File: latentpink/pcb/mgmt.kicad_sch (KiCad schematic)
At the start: 82 parts, among them J10 XILINX_JTAG, J11 FAN_01, J12 FAN_01, J15 CONN_01X03, J16 JUMPER_0402_SPDT, J17 JUMPER_0402_SPDT, J23 PMOD_HOST, J7 RJ45, U2 XC7K160T-2FBG484C, U20 AT24MAC402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

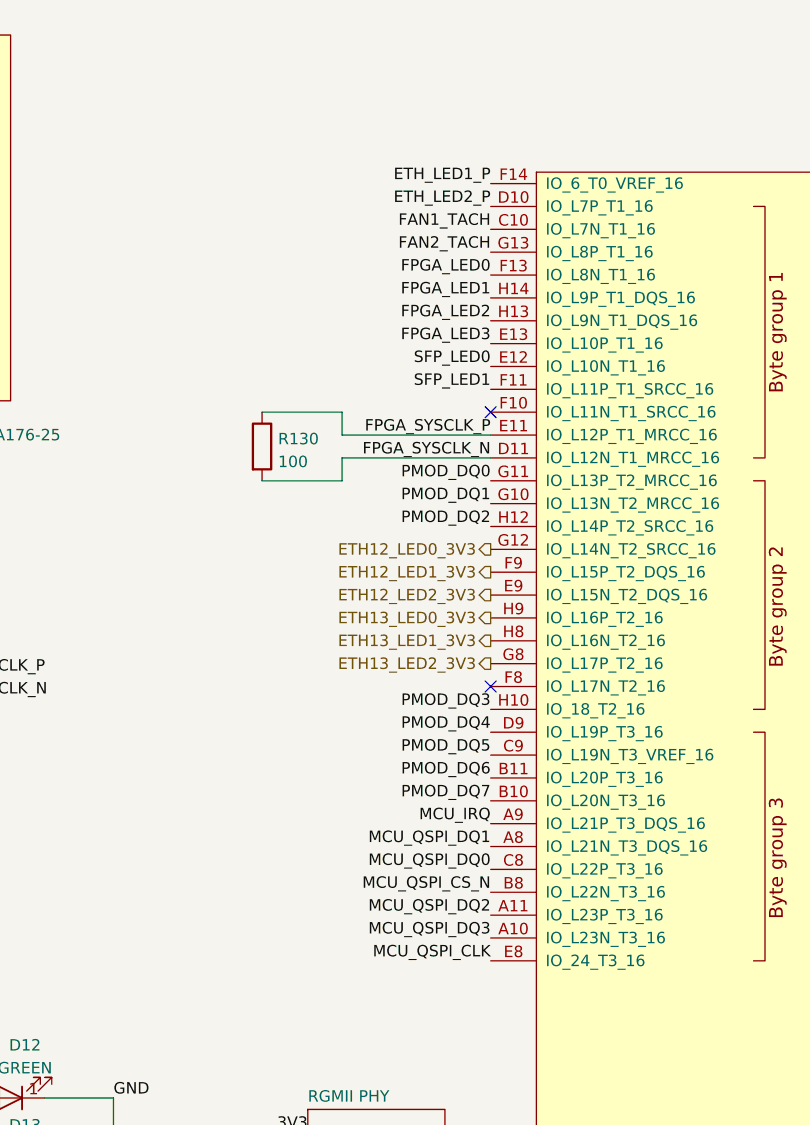
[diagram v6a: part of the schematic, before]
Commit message: Lots more layout of low speed stuff and power. Partial layout of 1.2V supply. Initial RGMII escape routing.
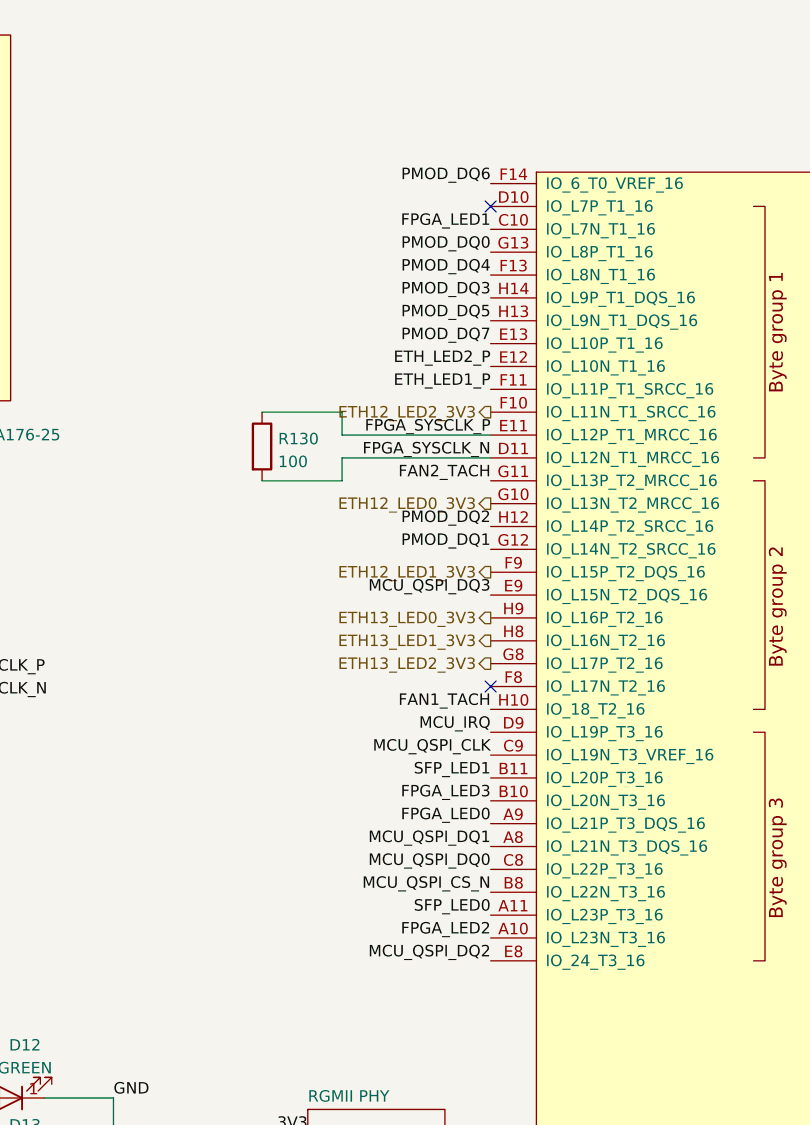
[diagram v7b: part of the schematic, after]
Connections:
- net ETH12_LED0_3V3: now also U2.G10 (IO_L13N_T2_MRCC_16); no longer U2.G12 (IO_L14N_T2_SRCC_16)
- net ETH12_LED2_3V3: now also U2.F10 (IO_L11N_T1_SRCC_16); no longer U2.E9 (IO_L15N_T2_DQS_16)
- net ETH_LED1_P: now also U2.F11 (IO_L11P_T1_SRCC_16); no longer U2.F14 (IO_6_T0_VREF_16)
- net ETH_LED2_P: now also U2.E12 (IO_L10N_T1_16); no longer U2.D10 (IO_L7P_T1_16)
- net FAN1_TACH: now also U2.H10 (IO_18_T2_16); no longer U2.C10 (IO_L7N_T1_16)
- net FAN2_TACH: now also U2.G11 (IO_L13P_T2_MRCC_16); no longer U2.G13 (IO_L8P_T1_16)
- net FPGA_LED0: now also U2.A9 (IO_L21P_T3_DQS_16); no longer U2.F13 (IO_L8N_T1_16)
- net FPGA_LED1: now also U2.C10 (IO_L7N_T1_16); no longer U2.H14 (IO_L9P_T1_DQS_16)
- net FPGA_LED2: now also U2.A10 (IO_L23N_T3_16); no longer U2.H13 (IO_L9N_T1_DQS_16)
- net FPGA_LED3: now also U2.B10 (IO_L20N_T3_16); no longer U2.E13 (IO_L10P_T1_16)
- net MCU_IRQ: now also U2.D9 (IO_L19P_T3_16); no longer U2.A9 (IO_L21P_T3_DQS_16)
- net MCU_QSPI_CLK: now also U2.C9 (IO_L19N_T3_VREF_16); no longer U2.E8 (IO_24_T3_16)
- net MCU_QSPI_DQ2: now also U2.E8 (IO_24_T3_16); no longer U2.A11 (IO_L23P_T3_16)
- net MCU_QSPI_DQ3: now also U2.E9 (IO_L15N_T2_DQS_16); no longer U2.A10 (IO_L23N_T3_16)
- net PMOD_DQ0: now also U2.G13 (IO_L8P_T1_16); no longer U2.G11 (IO_L13P_T2_MRCC_16)
- net PMOD_DQ1: now also U2.G12 (IO_L14N_T2_SRCC_16); no longer U2.G10 (IO_L13N_T2_MRCC_16)
- net PMOD_DQ3: now also U2.H14 (IO_L9P_T1_DQS_16); no longer U2.H10 (IO_18_T2_16)
- net PMOD_DQ4: now also U2.F13 (IO_L8N_T1_16); no longer U2.D9 (IO_L19P_T3_16)
- net PMOD_DQ5: now also U2.H13 (IO_L9N_T1_DQS_16); no longer U2.C9 (IO_L19N_T3_VREF_16)
- net PMOD_DQ6: now also U2.F14 (IO_6_T0_VREF_16); no longer U2.B11 (IO_L20P_T3_16)
- net PMOD_DQ7: now also U2.E13 (IO_L10P_T1_16); no longer U2.B10 (IO_L20N_T3_16)
- net SFP_LED0: now also U2.A11 (IO_L23P_T3_16); no longer U2.E12 (IO_L10N_T1_16)
- net SFP_LED1: now also U2.B11 (IO_L20P_T3_16); no longer U2.F11 (IO_L11P_T1_SRCC_16)
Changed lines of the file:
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@@
   (paper "A3")
   (title_block
-    (date "2023-05-31")
+    (date "2023-06-01")
     (rev "0.1")
     (company "Antikernel Labs")
@@
   (no_connect (at 260.35 60.96))
   (no_connect (at 214.63 86.36))
+  (no_connect (at 335.28 101.6))
   (no_connect (at 303.53 48.26))
   (no_connect (at 303.53 50.8))
@@
   (no_connect (at 260.35 114.3))
   (no_connect (at 214.63 101.6))
-  (no_connect (at 335.28 124.46))
   (no_connect (at 260.35 33.02))
   (no_connect (at 165.1 50.8))
@@
     (effects (font (size 1.27 1.27)) (justify right bottom))
   )
-  (label "ETH_LED1_P" (at 335.28 99.06 180)
-    (effects (font (size 1.27 1.27)) (justify right bottom))
-  )
-  (label "PMOD_DQ4" (at 335.28 160.02 180)
+  (label "ETH_LED1_P" (at 335.28 121.92 180)
+    (effects (font (size 1.27 1.27)) (justify right bottom))
+  )
+  (label "PMOD_DQ4" (at 335.28 109.22 180)
     (effects (font (size 1.27 1.27)) (justify right bottom))
   )
@@
     (effects (font (size 1.27 1.27)) (justify left bottom))
   )
-  (label "FPGA_LED0" (at 335.28 109.22 180)
+  (label "FPGA_LED0" (at 335.28 170.18 180)
     (effects (font (size 1.27 1.27)) (justify right bottom))
   )
@@
     (effects (font (size 1.27 1.27)) (justify right bottom))
   )
-  (label "PMOD_DQ6" (at 335.28 165.1 180)
+  (label "PMOD_DQ6" (at 335.28 99.06 180)
     (effects (font (size 1.27 1.27)) (justify right bottom))
   )
@@
     (effects (font (size 1.27 1.27)) (justify right bottom))
   )
-  (label "SFP_LED1" (at 335.28 121.92 180)
+  (label "SFP_LED1" (at 335.28 165.1 180)
     (effects (font (size 1.27 1.27)) (justify right bottom))
   )
@@
     (effects (font (size 1.27 1.27)) (justify right bottom))
   )
-  (label "ETH_LED2_P" (at 335.28 101.6 180)
+  (label "ETH_LED2_P" (at 335.28 119.38 180)
     (effects (font (size 1.27 1.27)) (justify right bottom))
   )
@@
     (effects (font (size 1.27 1.27)) (justify right bottom))
   )
-  (label "FPGA_LED2" (at 335.28 114.3 180)
+  (label "FPGA_LED2" (at 335.28 182.88 180)
     (effects (font (size 1.27 1.27)) (justify right bottom))
   )
@@
     (effects (font (size 1.27 1.27)) (justify right bottom))
   )
-  (label "PMOD_DQ1" (at 335.28 134.62 180)
+  (label "PMOD_DQ1" (at 335.28 139.7 180)
     (effects (font (size 1.27 1.27)) (justify right bottom))
   )
@@
     (effects (font (size 1.27 1.27)) (justify right bottom))
   )
-  (label "PMOD_DQ3" (at 335.28 157.48 180)
+  (label "PMOD_DQ3" (at 335.28 111.76 180)
     (effects (font (size 1.27 1.27)) (justify right bottom))
   )
@@
     (effects (font (size 1.27 1.27)) (justify right bottom))
   )
-  (label "SFP_LED0" (at 335.28 119.38 180)
+  (label "SFP_LED0" (at 335.28 180.34 180)
     (effects (font (size 1.27 1.27)) (justify right bottom))
   )
@@
     (effects (font (size 1.27 1.27)) (justify right bottom))
   )
-  (label "PMOD_DQ7" (at 335.28 167.64 180)
+  (label "PMOD_DQ7" (at 335.28 116.84 180)
     (effects (font (size 1.27 1.27)) (justify right bottom))
   )
@@
     (effects (font (size 1.27 1.27)) (justify right bottom))
   )
-  (label "MCU_IRQ" (at 335.28 170.18 180)
+  (label "MCU_IRQ" (at 335.28 160.02 180)
     (effects (font (size 1.27 1.27)) (justify right bottom))
   )
@@
     (effects (font (size 1.27 1.27)) (justify right bottom))
   )
-  (label "MCU_QSPI_DQ2" (at 335.28 180.34 180)
-    (effects (font (size 1.27 1.27)) (justify right bottom))
-  )
-  (label "PMOD_DQ5" (at 335.28 162.56 180)
+  (label "MCU_QSPI_DQ2" (at 335.28 185.42 180)
+    (effects (font (size 1.27 1.27)) (justify right bottom))
+  )
+  (label "PMOD_DQ5" (at 335.28 114.3 180)
     (effects (font (size 1.27 1.27)) (justify right bottom))
   )
@@
     (effects (font (size 1.27 1.27)) (justify right bottom))
   )
-  (label "FAN1_TACH" (at 335.28 104.14 180)
-    (effects (font (size 1.27 1.27)) (justify right bottom))
-  )
-  (label "MCU_QSPI_CLK" (at 335.28 185.42 180)
+  (label "FAN1_TACH" (at 335.28 157.48 180)
+    (effects (font (size 1.27 1.27)) (justify right bottom))
+  )
+  (label "MCU_QSPI_CLK" (at 335.28 162.56 180)
     (effects (font (size 1.27 1.27)) (justify right bottom))
   )
@@
     (effects (font (size 1.27 1.27)) (justify left bottom))
   )
-  (label "FPGA_LED3" (at 335.28 116.84 180)
-    (effects (font (size 1.27 1.27)) (justify right bottom))
-  )
-  (label "FPGA_LED1" (at 335.28 111.76 180)
+  (label "FPGA_LED3" (at 335.28 167.64 180)
+    (effects (font (size 1.27 1.27)) (justify right bottom))
+  )
+  (label "FPGA_LED1" (at 335.28 104.14 180)
     (effects (font (size 1.27 1.27)) (justify right bottom))
   )
@@
     (effects (font (size 1.27 1.27)) (justify right bottom))
   )
-  (label "MCU_QSPI_DQ3" (at 335.28 182.88 180)
+  (label "MCU_QSPI_DQ3" (at 335.28 144.78 180)
     (effects (font (size 1.27 1.27)) (justify right bottom))
   )
@@
     (effects (font (size 1.27 1.27)) (justify right bottom))
   )
-  (label "FAN2_TACH" (at 335.28 106.68 180)
+  (label "FAN2_TACH" (at 335.28 132.08 180)
     (effects (font (size 1.27 1.27)) (justify right bottom))
   )
@@
     (effects (font (size 1.27 1.27)) (justify right bottom))
   )
-  (label "PMOD_DQ0" (at 335.28 132.08 180)
+  (label "PMOD_DQ0" (at 335.28 106.68 180)
     (effects (font (size 1.27 1.27)) (justify right bottom))
   )
@@
     (effects (font (size 1.27 1.27)) (justify right))
   )
-  (hierarchical_label "ETH12_LED0_3V3" (shape output) (at 335.28 139.7 180)
+  (hierarchical_label "ETH12_LED0_3V3" (shape output) (at 335.28 134.62 180)
     (effects (font (size 1.27 1.27)) (justify right))
   )
@@
     (effects (font (size 1.27 1.27)) (justify right))
   )
-  (hierarchical_label "ETH12_LED2_3V3" (shape output) (at 335.28 144.78 180)
-    (effects (font (size 1.27 1.27)) (justify right))
-  )
+  (hierarchical_label "ETH12_LED2_3V3" (shape output) (at 335.28 124.46 180)
+    (effects (font (size 1.27 1.27)) (justify right))
+  )

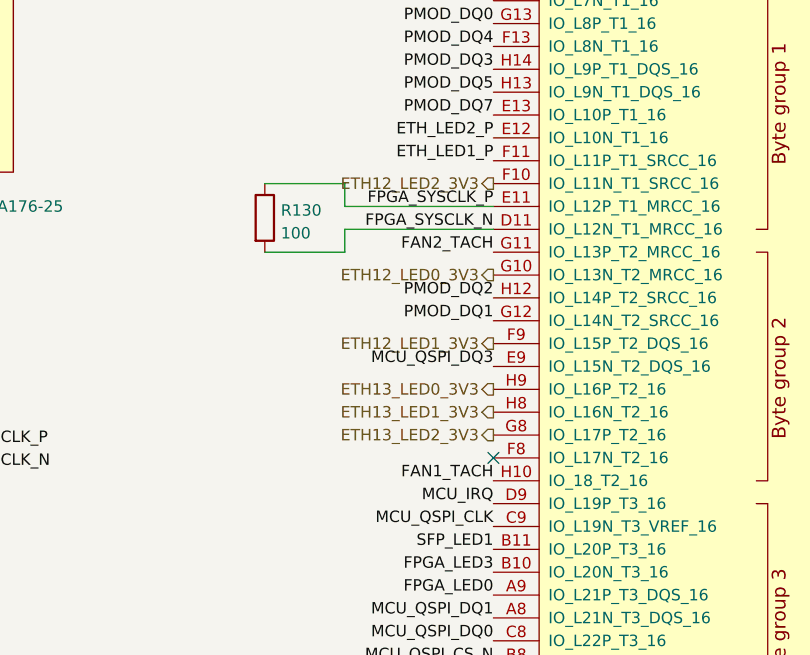
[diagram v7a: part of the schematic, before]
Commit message: Routing of northwest corner
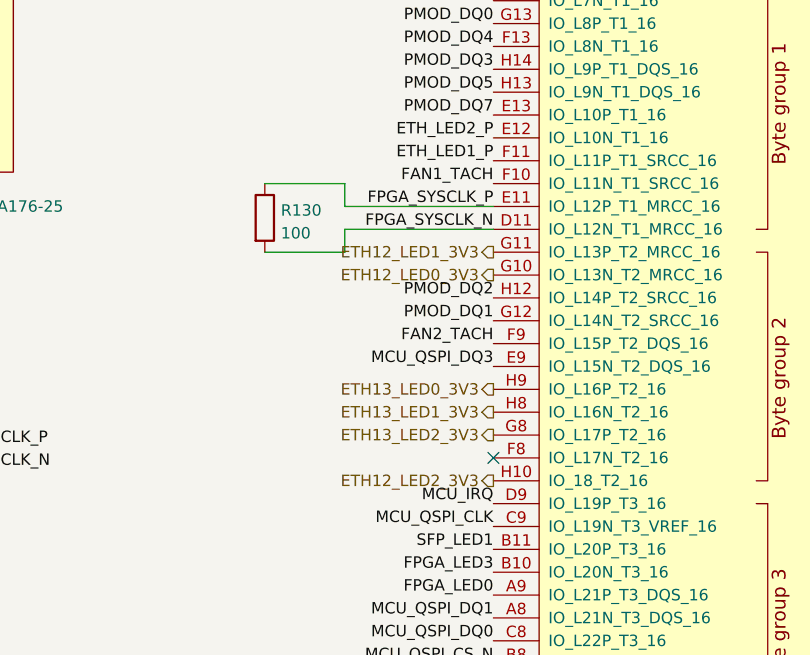
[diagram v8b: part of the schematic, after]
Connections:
- net ETH12_LED1_3V3: now also U2.G11 (IO_L13P_T2_MRCC_16); no longer U2.F9 (IO_L15P_T2_DQS_16)
- net ETH12_LED2_3V3: now also U2.H10 (IO_18_T2_16); no longer U2.F10 (IO_L11N_T1_SRCC_16)
- net FAN1_TACH: now also U2.F10 (IO_L11N_T1_SRCC_16); no longer U2.H10 (IO_18_T2_16)
- net FAN2_TACH: now also U2.F9 (IO_L15P_T2_DQS_16); no longer U2.G11 (IO_L13P_T2_MRCC_16)
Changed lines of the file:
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@@
     (effects (font (size 1.27 1.27)) (justify right bottom))
   )
-  (label "FAN1_TACH" (at 335.28 157.48 180)
+  (label "FAN1_TACH" (at 335.28 124.46 180)
     (effects (font (size 1.27 1.27)) (justify right bottom))
   )
@@
     (effects (font (size 1.27 1.27)) (justify right bottom))
   )
-  (label "FAN2_TACH" (at 335.28 132.08 180)
+  (label "FAN2_TACH" (at 335.28 142.24 180)
     (effects (font (size 1.27 1.27)) (justify right bottom))
   )
@@
     (effects (font (size 1.27 1.27)) (justify right))
   )
-  (hierarchical_label "ETH12_LED1_3V3" (shape output) (at 335.28 142.24 180)
+  (hierarchical_label "ETH12_LED1_3V3" (shape output) (at 335.28 132.08 180)
     (effects (font (size 1.27 1.27)) (justify right))
   )
@@
     (effects (font (size 1.27 1.27)) (justify right))
   )
-  (hierarchical_label "ETH12_LED2_3V3" (shape output) (at 335.28 124.46 180)
+  (hierarchical_label "ETH12_LED2_3V3" (shape output) (at 335.28 157.48 180)
     (effects (font (size 1.27 1.27)) (justify right))
   )
